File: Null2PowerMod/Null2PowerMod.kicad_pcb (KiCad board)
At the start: 2 copper layers, 18 x 28 mm, 33 parts, among them J1 USB_C_Receptacle_USB2.0, J2 JST 2-PH, J3 JP2, J5 Conn_01x01, J6 Conn_01x01, U1 MCP73871, U2 TPS61030PWP, U3 MMUN2133LT1G

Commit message: Fully routed
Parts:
- moved R9 70.0 mm to (99.6, 57.7), turned to -90 degrees
- moved C2 68.5 mm to (108.2, 45.7)
- moved C6 65.8 mm to (110.2, 49.3)
- moved C5 63.3 mm to (110.2, 50.5)
- moved R12 60.6 mm to (96.6, 59.7)
- moved R1 57.2 mm to (107.4, 50.0), turned to 90 degrees
- moved R13 52.2 mm to (106.9, 43.2)
- moved R8 51.4 mm to (98.3, 57.4)
- moved R7 50.1 mm to (109.2, 58.2), turned to 90 degrees
- moved L1 48.8 mm to (98.5, 45.5)
- moved C4 48.0 mm to (108.2, 46.7)
- moved R4 37.9 mm to (100.3, 48.0), turned to 180 degrees
- moved R3 36.4 mm to (108.5, 50.0), turned to 90 degrees
- moved C3 35.8 mm to (97.5, 56.4), turned to 90 degrees
- moved R10 32.0 mm to (110.0, 55.9), turned to 180 degrees
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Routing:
- net GND: track 48.4 -> 110.3 mm, vias 1 -> 4
- net +5V: track 21.7 -> 69.6 mm, vias 0 -> 1
- net VLIPO: track 19.4 -> 64.9 mm, vias 1 -> 3
- net VBUS: track 21.4 -> 63.4 mm, vias 2 -> 5
- net Net-(D4-Pad2): track 0.00 -> 23.7 mm
- net Net-(D1-Pad1): track 0.00 -> 22.7 mm, vias 0 -> 4
- net Net-(R6-Pad1): track 0.00 -> 19.0 mm, vias 0 -> 2
- net unconnected-(J1-PadS1): track 0.00 -> 15.4 mm
- net Net-(L1-Pad1): track 0.00 -> 12.0 mm
- net Net-(R8-Pad2): track 0.00 -> 2.90 mm
- net Net-(R3-Pad2): track 0.00 -> 2.84 mm
- net Net-(R7-Pad2): track 0.00 -> 2.09 mm
- net Net-(D2-Pad1): track 0.00 -> 1.50 mm
- net Net-(R1-Pad2): track 0.00 -> 1.46 mm
- net Net-(R13-Pad1): track 0.00 -> 1.36 mm
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
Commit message: Feedback changes
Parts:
- added J6: Conn_01x01, Connector_PinHeader_2.54mm:PinHeader_1x01_P2.54mm_Vertical, F.Cu at (96.3, 65.8)
- renumbered C5 to C1, C3 to C2, C6 to C3, C2 to C4, C4 to C5, C1 to C6, D3 to D1, D1 to D3, J6 to J1, J1 to J2, J5 to J3, J3 to J4, J2 to J5, R4 to R1, R9 to R10, R10 to R11, R6 to R13, R3 to R2, R1 to R3, R7 to R4, R11 to R5, R13 to R6, R5 to R7, R2 to R8, R8 to R9, U3 to U1, U1 to U3
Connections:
- C1 pad 1: +5V -> VBUS
- C3 pad 1: +5V -> VLIPO
- C5 pad 1: VLIPO -> +5V
- C6 pad 1: VBUS -> +5V
- D1 pad 1: GND -> Net-(D1-Pad1)
- D1 pad 2: Net-(D3-Pad2) -> VBUS
- D3 pad 1: Net-(D1-Pad1) -> GND
- D3 pad 2: VBUS -> Net-(D3-Pad2)
- J1 pad 1: GND -> (no net)
- J2 pad A1: GND -> (no net)
- J2 pad A12: GND -> (no net)
- J2 pad A4: VBUS -> (no net)
- J2 pad A5: unconnected-(J1-PadA5) -> (no net)
- J2 pad A6: unconnected-(J1-PadA6) -> (no net)
- J2 pad A7: unconnected-(J1-PadA7) -> (no net)
- J2 pad A8: unconnected-(J1-PadA8) -> (no net)
- J2 pad A9: VBUS -> (no net)
- J2 pad B1: GND -> (no net)
- J2 pad B12: GND -> (no net)
- J2 pad B4: VBUS -> (no net)
- J2 pad B5: unconnected-(J1-PadB5) -> (no net)
- J2 pad B6: unconnected-(J1-PadB6) -> (no net)
- J2 pad B7: unconnected-(J1-PadB7) -> (no net)
- J2 pad B8: unconnected-(J1-PadB8) -> (no net)
- J2 pad B9: VBUS -> (no net)
- J2 pad S1: unconnected-(J1-PadS1) -> (no net)
- J3 pad 1: +5V -> VLIPO
- J5 pad 1: VLIPO -> +5V
- J5 pad 2: GND -> (no net)
- R1 pad 1: VBUS -> GND
- R1 pad 2: Net-(R2-Pad2) -> Net-(R1-Pad2)
- R10 pad 1: Net-(R8-Pad2) -> +5V
- R10 pad 2: GND -> Net-(R10-Pad2)
- R11 pad 1: +5V -> Net-(R10-Pad2)
- R11 pad 2: Net-(R10-Pad2) -> GND
- R13 pad 1: Net-(R6-Pad1) -> Net-(R13-Pad1)
- R13 pad 2: Net-(D2-Pad1) -> Net-(D4-Pad2)
- R2 pad 2: Net-(R3-Pad2) -> Net-(R2-Pad2)
- R3 pad 2: Net-(R1-Pad2) -> Net-(R3-Pad2)
- R4 pad 1: VLIPO -> VBUS
- R4 pad 2: Net-(R7-Pad2) -> Net-(R2-Pad2)
- R5 pad 1: Net-(R10-Pad2) -> Net-(R5-Pad1)
- R5 pad 2: GND -> Net-(D1-Pad1)
- R6 pad 1: Net-(R13-Pad1) -> Net-(R6-Pad1)
- R6 pad 2: Net-(D4-Pad2) -> Net-(D2-Pad1)
- R7 pad 1: Net-(R5-Pad1) -> VLIPO
- R7 pad 2: Net-(D1-Pad1) -> Net-(R7-Pad2)
- R8 pad 1: GND -> VLIPO
- R8 pad 2: Net-(R2-Pad2) -> Net-(R8-Pad2)
- R9 pad 1: VLIPO -> Net-(R8-Pad2)
- R9 pad 2: Net-(R8-Pad2) -> GND
- U1 pad 1: /LB0 -> VLIPO
- U1 pad 2: Net-(R13-Pad1) -> Net-(R2-Pad2)
- U1 pad 3: VLIPO -> VBUS
- U3 pad 1: VLIPO -> /LB0
- U3 pad 10: GND -> (no net)
- U3 pad 11: GND -> (no net)
- U3 pad 12: Net-(R1-Pad2) -> (no net)
- U3 pad 13: Net-(R3-Pad2) -> (no net)
- U3 pad 14: VLIPO -> (no net)
- U3 pad 15: VLIPO -> (no net)
- U3 pad 16: VLIPO -> (no net)
- U3 pad 17: VBUS -> (no net)
- U3 pad 18: VBUS -> (no net)
- U3 pad 19: VBUS -> (no net)
- U3 pad 2: Net-(R2-Pad2) -> Net-(R13-Pad1)
- U3 pad 20: VLIPO -> (no net)
- U3 pad 21: GND -> (no net)
- U3 pad 3: VBUS -> VLIPO
- U3 pad 4: VBUS -> (no net)
- U3 pad 5: Net-(TH1-Pad2) -> (no net)
- U3 pad 6: unconnected-(U1-Pad6) -> (no net)
- U3 pad 7: Net-(R5-Pad1) -> (no net)
- U3 pad 8: Net-(R6-Pad1) -> (no net)
- U3 pad 9: VBUS -> (no net)
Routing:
- net Net-(D4-Pad2): track 23.7 -> 0.00 mm
- net Net-(D2-Pad1): track 1.50 -> 25.2 mm
- net GND: track 110.3 -> 131.8 mm, vias 4 -> 5
- net Net-(D1-Pad1): track 22.7 -> 1.45 mm, vias 4 -> 3
- net Net-(R6-Pad1): track 19.0 -> 1.36 mm
- net Net-(R13-Pad1): track 1.36 -> 19.0 mm
- net unconnected-(J1-PadS1): track 15.4 -> 0.00 mm
- net (no net): track 0.00 -> 15.4 mm
- net Net-(R8-Pad2): track 2.90 -> 0.00 mm
- net +5V: track 69.6 -> 66.7 mm
- net Net-(R10-Pad2): track 2.54 -> 0.00 mm
- net Net-(R1-Pad2): track 1.46 -> 3.76 mm
- net Net-(R7-Pad2): track 2.09 -> 0.00 mm
- net Net-(R3-Pad2): track 2.84 -> 1.46 mm
- net Net-(R5-Pad1): track 1.25 -> 2.54 mm
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
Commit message: implementing feedback
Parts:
- removed J4: JP2, Connector_PinHeader_1.00mm:PinHeader_1x08_P1.00mm_Vertical
- removed U3: MCP73871, Package_DFN_QFN:QFN-20-1EP_4x4mm_P0.5mm_EP2.5x2.5mm
- U1: value MMUN2133LT1G -> MCP73871; footprint MMUN2133LT1G:MMUN2133LT1G -> Package_DFN_QFN:QFN-20-1EP_4x4mm_P0.5mm_EP2.5x2.5mm
- moved U1 5.22 mm to (104.1, 49.4), turned to 0 degrees
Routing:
- net +5V: track 66.7 -> 128.9 mm
- net VBUS: track 62.2 -> 0.00 mm
- net /LB0: track 20.9 -> 12.9 mm
- net VLIPO: track 65.9 -> 74.0 mm
- net GND: track 131.8 -> 135.8 mm
- net Net-(R8-Pad2): track 0.00 -> 3.76 mm
- net Net-(R1-Pad2): track 3.76 -> 0.00 mm
- net Net-(R5-Pad1): track 2.54 -> 0.00 mm
- net Net-(D4-Pad2): track 0.00 -> 1.50 mm
- net Net-(D2-Pad1): track 25.2 -> 23.7 mm
- net Net-(D1-Pad1): track 1.45 -> 0.00 mm

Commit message: wtf happened to the schematic?
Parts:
- added U3: MMUN2133LT1G, MMUN2133LT1G:MMUN2133LT1G, F.Cu at (89.0, 44.6)
- moved J6 32.5 mm to (115.5, 39.6)
- moved D1 32.2 mm to (119.2, 38.2)
- moved C6 26.0 mm to (121.7, 38.2)
- moved C2 23.3 mm to (117.7, 44.6), turned to 0 degrees
- moved J1 22.8 mm to (95.9, 57.7)
- moved J5 22.4 mm to (87.5, 57.1)
- moved J2 22.3 mm to (98.1, 38.9)
- moved R9 21.2 mm to (115.2, 44.6)
- moved R5 20.8 mm to (121.5, 39.9), turned to 0 degrees
- moved L1 18.7 mm to (117.0, 42.8)
- moved D4 18.4 mm to (114.6, 42.8)
- moved R1 15.0 mm to (115.2, 46.3), turned to 0 degrees
- moved D3 13.4 mm to (105.7, 51.5), turned to 0 degrees
- moved R8 13.4 mm to (112.8, 46.3)
- moved J3 13.4 mm to (109.2, 45.9)
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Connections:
- C2 pad 1: VLIPO -> Net-(C2-Pad1)
- C3 pad 1: VLIPO -> Net-(C3-Pad1)
- C4 pad 1: VLIPO -> Net-(C3-Pad1)
- J3 pad 1: VLIPO -> VBUS
- L1 pad 2: VLIPO -> VBAT
- R7 pad 1: VLIPO -> unconnected-(R7-Pad1)
- R8 pad 1: VLIPO -> Net-(C3-Pad1)
- U1 pad 1: VLIPO -> Net-(U1-Pad1)
- U1 pad 14: VLIPO -> Net-(C2-Pad1)
- U1 pad 15: VLIPO -> Net-(C2-Pad1)
- U1 pad 16: VLIPO -> Net-(C2-Pad1)
- U1 pad 20: VLIPO -> Net-(U1-Pad1)
- U2 pad 6: VLIPO -> Net-(C3-Pad1)
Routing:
- net GND: track 135.8 -> 0.00 mm, vias 5 -> 0
- net +5V: track 128.9 -> 0.00 mm, vias 1 -> 0
- net VLIPO: track 74.0 -> 0.00 mm, vias 1 -> 0
- net Net-(D2-Pad1): track 23.7 -> 0.00 mm
- net Net-(R13-Pad1): track 19.0 -> 0.00 mm
- net (no net): track 15.4 -> 0.00 mm
- net /LB0: track 12.9 -> 0.00 mm, vias 1 -> 0
- net Net-(L1-Pad1): track 11.0 -> 0.00 mm
- net Net-(R2-Pad2): track 4.93 -> 0.00 mm
- net Net-(R8-Pad2): track 3.76 -> 0.00 mm
- net Net-(D4-Pad2): track 1.50 -> 0.00 mm
- net Net-(R3-Pad2): track 1.46 -> 0.00 mm
- net Net-(R6-Pad1): track 1.36 -> 0.00 mm, vias 2 -> 0
- net Net-(TH1-Pad2): track 1.34 -> 0.00 mm
- net Net-(D3-Pad2): track 1.31 -> 0.00 mm
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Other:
- board outline removed

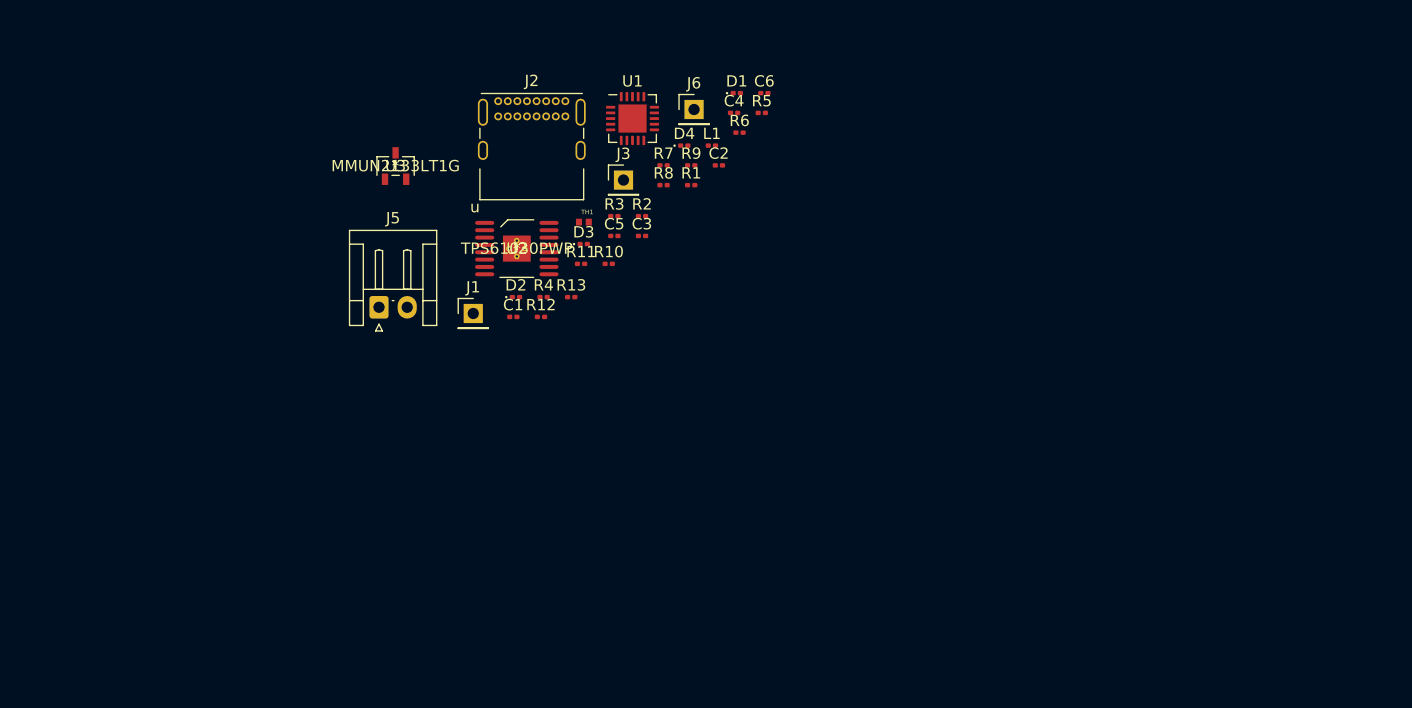
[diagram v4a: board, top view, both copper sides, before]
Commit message: updating schematic, re-starting the pcb completly
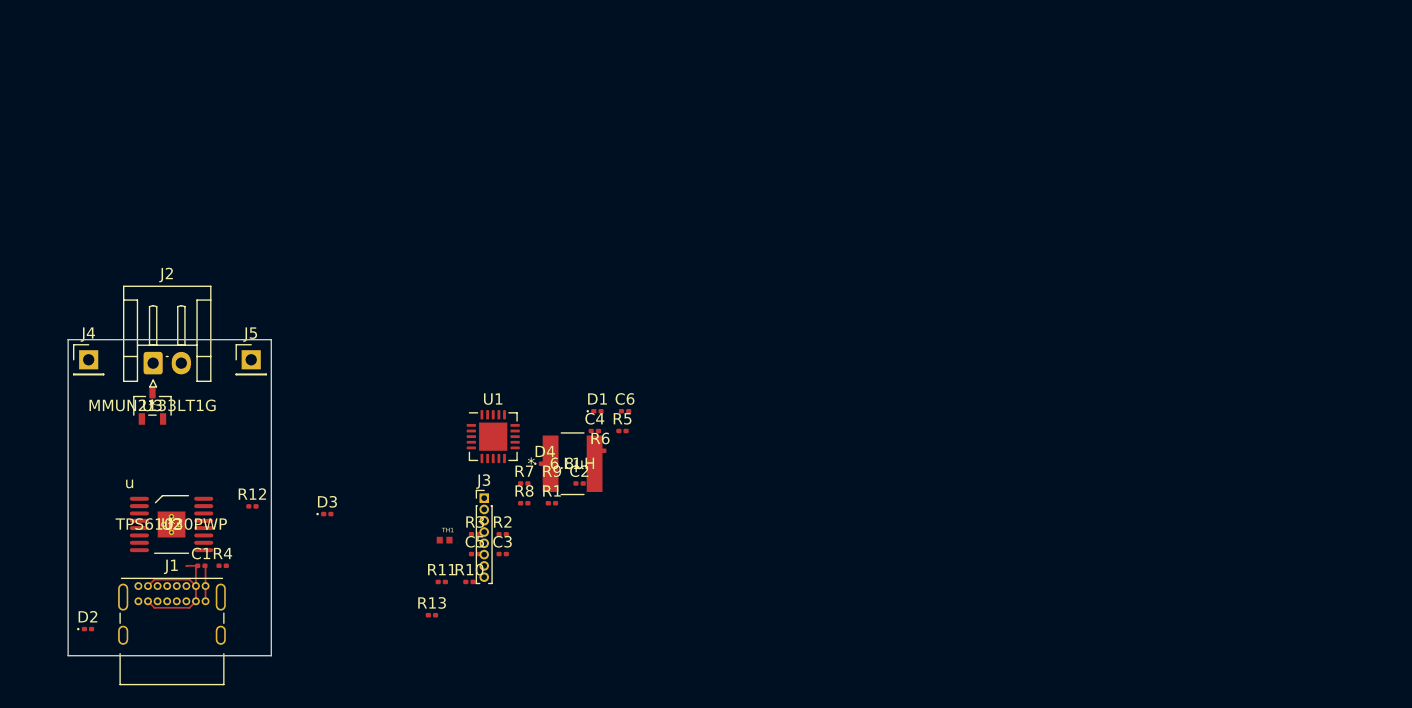
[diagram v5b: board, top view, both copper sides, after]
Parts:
- removed J6: Conn_01x01, Connector_PinHeader_2.54mm:PinHeader_1x01_P2.54mm_Vertical
- added J4: Conn_01x01, Connector_PinHeader_2.54mm:PinHeader_1x01_P2.54mm_Vertical, F.Cu at (61.8, 61.8)
- J1: value Conn_01x01 -> USB_C_Receptacle_USB2.0; footprint Connector_PinHeader_2.54mm:PinHeader_1x01_P2.54mm_Vertical -> Connector_USB:USB_C_Receptacle_GCT_USB4085
- J2: value USB_C_Receptacle_USB2.0 -> Conn_01x02_Female; footprint Connector_USB:USB_C_Receptacle_GCT_USB4085 -> Connector_JST:JST_EH_S2B-EH_1x02_P2.50mm_Horizontal
- J3: value Conn_01x01 -> Conn_01x08; footprint Connector_PinHeader_2.54mm:PinHeader_1x01_P2.54mm_Vertical -> Connector_PinHeader_1.00mm:PinHeader_1x08_P1.00mm_Vertical
- J5: value JST 2-PH -> Conn_01x01; footprint Connector_JST:JST_EH_S2B-EH_1x02_P2.50mm_Horizontal -> Connector_PinHeader_2.54mm:PinHeader_1x01_P2.54mm_Vertical
- L1: footprint Inductor_SMD:L_0201_0603Metric -> VLC5045:VLC5045T-4R7M
- moved D2 48.0 mm to (61.8, 85.6)
- moved U2 39.2 mm to (69.2, 76.4)
- moved J2 38.4 mm to (67.5, 62.1)
- moved J1 38.2 mm to (66.2, 81.8)
- moved R4 37.1 mm to (73.7, 80.0)
- moved C1 35.4 mm to (71.8, 80.0)
- moved D3 33.0 mm to (83.0, 75.5)
- moved C4 30.8 mm to (106.7, 68.1)
- moved C6 30.8 mm to (109.3, 66.3)
- moved D1 30.8 mm to (106.9, 66.3)
- moved J3 30.8 mm to (96.9, 74.0)
- moved R5 30.8 mm to (109.1, 68.1)
- moved R6 30.8 mm to (107.1, 69.8)
- moved TH1 30.8 mm to (93.3, 77.8)
- moved U1 30.8 mm to (97.7, 68.6)
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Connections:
- C2 pad 1: Net-(C2-Pad1) -> VLIPO
- C3 pad 1: Net-(C3-Pad1) -> VBAT
- C4 pad 1: Net-(C3-Pad1) -> VBAT
- J5 pad 1: +5V -> GND
- R7 pad 1: unconnected-(R7-Pad1) -> VBAT
- R7 pad 2: Net-(R7-Pad2) -> /Enable
- R8 pad 1: Net-(C3-Pad1) -> VBAT
- U1 pad 1: Net-(U1-Pad1) -> VBAT
- U1 pad 14: Net-(C2-Pad1) -> VLIPO
- U1 pad 15: Net-(C2-Pad1) -> VLIPO
- U1 pad 16: Net-(C2-Pad1) -> VLIPO
- U1 pad 20: Net-(U1-Pad1) -> VBAT
- U2 pad 17: unconnected-(U2-Pad17) -> GND
- U2 pad 6: Net-(C3-Pad1) -> VBAT
- U2 pad 9: Net-(R7-Pad2) -> /Enable
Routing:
- net VBUS: track 0.00 -> 13.7 mm
- net GND: track 0.00 -> 3.17 mm
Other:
- board outline added: 18 x 28 mm

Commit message: Refreshed ideas for next milestone
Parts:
- removed TH1: 15K, Libraries:THRMC1005X55N
- added NT1: NetTie_2, NetTie:NetTie-2_SMD_Pad0.5mm, F.Cu at (89.1, 64.7)
- added REF**: PinHeader_1x01_P2.54mm_Vertical, Connector_PinHeader_2.54mm:PinHeader_1x01_P2.54mm_Vertical, F.Cu at (76.2, 86.2)
- added REF**: PinHeader_1x01_P2.54mm_Vertical, Connector_PinHeader_2.54mm:PinHeader_1x01_P2.54mm_Vertical, F.Cu at (61.8, 86.2)
- added RT1: NCP15XW153J03RC, NCP15XW153J03RC:THRMC1005X55N, F.Cu at (93.2, 57.6)
- C3: value 100μF -> 2.2 μF
- C4: value 10μF -> 220μF; footprint Capacitor_SMD:C_0201_0603Metric -> Capacitor_Tantalum_SMD:CP_EIA-2012-15_AVX-P
- C5: value 0.1μF -> 10μF
- D1: value BLUE -> Orange
- D2: value Green -> RED
- D3: value Orange -> BLUE
- D4: value RED -> Green
- J2: value Conn_01x02_Female -> Conn_01x08; footprint Connector_JST:JST_EH_S2B-EH_1x02_P2.50mm_Horizontal -> Connector_PinHeader_1.00mm:PinHeader_1x08_P1.00mm_Vertical
- J3: value Conn_01x08 -> Conn_01x01; footprint Connector_PinHeader_1.00mm:PinHeader_1x08_P1.00mm_Vertical -> Connector_PinHeader_2.54mm:PinHeader_1x01_P2.54mm_Vertical
- J5: value Conn_01x01 -> Conn_01x02_Female; footprint Connector_PinHeader_2.54mm:PinHeader_1x01_P2.54mm_Vertical -> Connector_JST:JST_EH_S2B-EH_1x02_P2.50mm_Horizontal
- L1: value 6.8μH -> VLC5045T-330M; footprint VLC5045:VLC5045T-4R7M -> ul_VLC5045T-330M:VLC5045T-330M
- R1: value 270k -> 390kΩ
- R10: value 340k -> 100k
- R11: value 1.07MΩ -> 200k
- R12: value 1k -> 200k
- R13: value 1K -> 1k
- R2: value 1k -> 390kΩ
- R3: value 100k -> 1.05MΩ
- R4: value 200k -> 180kΩ
- R5: value 200k -> 1MΩ
- R8: value 100k -> 270k
- R9: value 1.87M -> 1k
- U1: value MCP73871 -> TPS61030PWP; footprint Package_DFN_QFN:QFN-20-1EP_4x4mm_P0.5mm_EP2.5x2.5mm -> ul_TPS61030PWP:TPS61030PWP
- U2: value TPS61030PWP -> MMUN2133LT1G; footprint TPS61030PWP:TPS61030PWP -> ul_MMUN2133LT1G:MMUN2133LT1G
- U3: value MMUN2133LT1G -> MCP73871; footprint MMUN2133LT1G:MMUN2133LT1G -> Package_DFN_QFN:QFN-20-1EP_4x4mm_P0.5mm_EP2.5x2.5mm
- moved L1 41.8 mm to (62.9, 71.0)
- moved D1 32.6 mm to (76.0, 76.8)
- moved C4 31.2 mm to (75.6, 64.7), turned to 180 degrees
- moved U1 29.8 mm to (69.0, 76.7)
- moved J3 24.0 mm to (76.3, 61.8)
- moved U2 12.3 mm to (80.7, 72.0)
- moved J2 10.8 mm to (76.9, 67.4)
- moved C1 8.97 mm to (80.8, 80.5)
- moved J5 8.77 mm to (67.5, 61.6)
- moved R12 8.42 mm to (83.8, 78.6)
- moved R4 8.15 mm to (80.9, 83.8)
- moved U3 5.59 mm to (70.9, 70.3), turned to 90 degrees
- moved R13 4.05 mm to (88.2, 84.5)
- moved J1 0.21 mm to (66.0, 81.9)
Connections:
- C2 pad 1: VLIPO -> Net-(C2-Pad1)
- C3 pad 1: VBAT -> +5V
- C4 pad 1: VBAT -> +5V
- C6 pad 1: +5V -> VLIPO
- D1 pad 1: Net-(D1-Pad1) -> GND
- D1 pad 2: VBUS -> Net-(D1-Pad2)
- D2 pad 1: Net-(D2-Pad1) -> GND
- D2 pad 2: VBUS -> Net-(D2-Pad2)
- D3 pad 1: GND -> Net-(D3-Pad1)
- D3 pad 2: Net-(D3-Pad2) -> VBUS
- D4 pad 1: GND -> Net-(D4-Pad1)
- D4 pad 2: Net-(D4-Pad2) -> VBUS
- J2 pad 1: VLIPO -> VBUS
- J2 pad 2: GND -> VLIPO
- J3 pad 1: VBUS -> +5V
- J4 pad 1: +5V -> GND
- J5 pad 1: GND -> VLIPO
- L1 pad 1: Net-(L1-Pad1) -> Net-(C2-Pad1)
- L1 pad 2: VBAT -> Net-(L1-Pad2)
- R1 pad 1: GND -> Net-(C2-Pad1)
- R10 pad 1: +5V -> GND
- R11 pad 1: Net-(R10-Pad2) -> VBUS
- R11 pad 2: GND -> Net-(R11-Pad2)
- R12 pad 1: +5V -> Net-(R12-Pad1)
- R12 pad 2: Net-(D3-Pad2) -> Net-(D3-Pad1)
- R13 pad 2: Net-(D4-Pad2) -> Net-(D4-Pad1)
- R2 pad 1: GND -> Net-(R1-Pad2)
- R2 pad 2: Net-(R2-Pad2) -> GND
- R3 pad 1: GND -> +5V
- R4 pad 1: VBUS -> Net-(R3-Pad2)
- R4 pad 2: Net-(R2-Pad2) -> GND
- R5 pad 1: Net-(R5-Pad1) -> +5V
- R5 pad 2: Net-(D1-Pad1) -> /LB0
- R6 pad 1: Net-(R6-Pad1) -> +5V
- R6 pad 2: Net-(D2-Pad1) -> Net-(D1-Pad2)
- R7 pad 1: VBAT -> Net-(R7-Pad1)
- R7 pad 2: /Enable -> Net-(D2-Pad2)
- R8 pad 1: VBAT -> GND
- R9 pad 1: Net-(R8-Pad2) -> GND
- R9 pad 2: GND -> Net-(R11-Pad2)
- U1 pad 1: VBAT -> Net-(L1-Pad2)
- U1 pad 10: GND -> /LB0
- U1 pad 12: Net-(R1-Pad2) -> Net-(R3-Pad2)
- U1 pad 13: Net-(R3-Pad2) -> +5V
- U1 pad 14: VLIPO -> +5V
- U1 pad 15: VLIPO -> +5V
- U1 pad 16: VLIPO -> unconnected-(U1-Pad16)
- U1 pad 17: VBUS -> GND
- U1 pad 2: Net-(R2-Pad2) -> Net-(L1-Pad2)
- U1 pad 3: VBUS -> GND
- U1 pad 4: VBUS -> GND
- U1 pad 5: Net-(TH1-Pad2) -> GND
- U1 pad 6: unconnected-(U1-Pad6) -> Net-(C2-Pad1)
- U1 pad 7: Net-(R5-Pad1) -> Net-(R1-Pad2)
- U1 pad 8: Net-(R6-Pad1) -> GND
- U1 pad 9: VBUS -> Net-(C2-Pad1)
- U2 pad 1: Net-(L1-Pad1) -> /LB0
- U2 pad 2: Net-(L1-Pad1) -> Net-(R7-Pad1)
- U2 pad 3: GND -> Net-(U2-Pad3)
- U3 pad 1: /LB0 -> Net-(U3-Pad1)
- U3 pad 2: Net-(R13-Pad1) -> Net-(R11-Pad2)
- U3 pad 3: VBAT -> VBUS
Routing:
- net +5V: track 0.00 -> 13.4 mm
- net GND: track 3.17 -> 6.34 mm
- net VBUS: track 13.7 -> 16.8 mm
- added copper zone on B.Cu, net GND
- added copper zone on F.Cu, net GND

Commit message: Redesigning pcb
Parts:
- removed NT1: NetTie_2, NetTie:NetTie-2_SMD_Pad0.5mm
- moved R6 45.0 mm to (63.4, 80.0), turned to 180 degrees
- moved C2 44.2 mm to (61.4, 78.0), turned to -90 degrees
- moved D4 42.5 mm to (61.9, 84.3)
- moved R1 42.0 mm to (61.0, 76.9), turned to 180 degrees
- moved C6 40.6 mm to (68.8, 64.1)
- moved R5 38.9 mm to (70.6, 73.6)
- moved R7 38.1 mm to (63.3, 81.4), turned to -90 degrees
- moved R2 37.9 mm to (60.6, 78.0), turned to -90 degrees
- moved R9 29.9 mm to (74.0, 80.5)
- moved R10 29.4 mm to (70.7, 65.8)
- moved R8 29.3 mm to (72.3, 66.2), turned to 180 degrees
- moved C3 28.3 mm to (70.5, 74.5)
- moved R13 27.4 mm to (60.8, 84.0), turned to -90 degrees
- moved RT1 26.3 mm to (71.6, 72.6)
- moved R3 25.0 mm to (71.0, 76.5)
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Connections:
- C2 pad 1: Net-(C2-Pad1) -> /Enable
- L1 pad 1: Net-(C2-Pad1) -> /Enable
- R1 pad 1: Net-(C2-Pad1) -> /Enable
- U1 pad 6: Net-(C2-Pad1) -> /Enable
- U1 pad 9: Net-(C2-Pad1) -> /Enable
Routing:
- net VBUS: track 16.8 -> 60.4 mm, vias 0 -> 3
- net GND: track 6.34 -> 43.0 mm
- net /Enable: track 0.00 -> 33.3 mm
- net +5V: track 13.4 -> 46.3 mm, vias 0 -> 2
- net Net-(R13-Pad1): track 0.00 -> 24.9 mm, vias 0 -> 2
- net Net-(R12-Pad1): track 0.00 -> 22.8 mm, vias 0 -> 2
- net VLIPO: track 0.00 -> 19.0 mm
- net /LB0: track 0.00 -> 15.2 mm, vias 0 -> 1
- net Net-(R7-Pad1): track 0.00 -> 14.1 mm
- net Net-(R11-Pad2): track 0.00 -> 12.6 mm, vias 0 -> 2
- net Net-(L1-Pad2): track 0.00 -> 9.59 mm
- net Net-(R1-Pad2): track 0.00 -> 4.94 mm
- net Net-(R3-Pad2): track 0.00 -> 3.62 mm
- net Net-(R8-Pad2): track 0.00 -> 1.95 mm
- net Net-(R10-Pad2): track 0.00 -> 1.86 mm
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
